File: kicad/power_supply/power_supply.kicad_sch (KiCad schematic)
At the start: 15 parts, among them J1 Conn_WallSocket_Earth, J2 Conn_01x03, J3 Conn_01x04_Pin, SW1 SW_SPST, T1 Transformer_SP_2S

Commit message: Commit
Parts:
- removed J2: Conn_01x03, symbol Connector_Generic:Conn_01x03
- removed J3: Conn_01x04_Pin, symbol Connector:Conn_01x04_Pin
- added C1, C20: 1u, Capacitor_SMD:C_0805_2012Metric_Pad1.18x1.45mm_HandSolder, symbol Device:C
- added C10, C17, C18: 47u, Capacitor_SMD:C_0805_2012Metric_Pad1.18x1.45mm_HandSolder, symbol Device:C
- added C19, C6, C8: 100n, Capacitor_SMD:C_0805_2012Metric_Pad1.18x1.45mm_HandSolder, symbol Device:C
- added C2, C5: 4u7, symbol Device:C
- added C3, C4: C, symbol Device:C
- added C7, C9: 10u, Capacitor_SMD:C_0805_2012Metric_Pad1.18x1.45mm_HandSolder, symbol Device:C
- added D1, D2, D3, D4: D_TVS, symbol Device:D_TVS
- added D6, D7: V<Vgs, symbol Device:D_Zener
- added FB1, FB2: FerriteBead, symbol Device:FerriteBead
- added HS1: Heatsink, symbol Mechanical:Heatsink
- added J2: USB_C_Receptacle_USB2.0, Connector_USB:USB_C_Receptacle_GCT_USB4085, symbol Connector:USB_C_Receptacle_USB2.0
- added J3: Conn_01x03, symbol Connector_Generic:Conn_01x03
- added J4: Conn_02x08_Odd_Even, Connector_PinSocket_2.54mm:PinSocket_2x08_P2.54mm_Vertical, symbol Connector_Generic:Conn_02x08_Odd_Even
- added JP1: Jumper_2_Open, Jumper:SolderJumper-2_P1.3mm_Open_Pad1.0x1.5mm, symbol Jumper:Jumper_2_Open
- added Q1, Q5: PMOS, symbol Simulation_SPICE:PMOS
- added Q2, Q6: NMOS, symbol Simulation_SPICE:NMOS
- added Q3: PNP, symbol Simulation_SPICE:PNP
- added Q4: NPN, symbol Simulation_SPICE:NPN
- added Q7: NPN, Package_TO_SOT_THT:TO-220-3_Vertical, symbol Simulation_SPICE:NPN
- added Q8: PNP, Package_TO_SOT_THT:TO-220-3_Vertical, symbol Simulation_SPICE:PNP
- added R1: 5.1k, Resistor_SMD:R_0805_2012Metric_Pad1.20x1.40mm_HandSolder, symbol Device:R
- added R10, R25, R7: 10k, Resistor_SMD:R_0805_2012Metric_Pad1.20x1.40mm_HandSolder, symbol Device:R
- added R11, R12: 1, symbol Device:R
- added R15, R16: 0R67, symbol Device:R
- added R17, R20: 33k, Resistor_SMD:R_0805_2012Metric_Pad1.20x1.40mm_HandSolder, symbol Device:R
- added R18, R19: 1k, Resistor_SMD:R_0805_2012Metric_Pad1.20x1.40mm_HandSolder, symbol Device:R
- added R2, R5: 1k5, Resistor_SMD:R_0805_2012Metric_Pad1.20x1.40mm_HandSolder, symbol Device:R
- added R21, R22: 3k3, Resistor_SMD:R_0805_2012Metric_Pad1.20x1.40mm_HandSolder, symbol Device:R
- added R23, R24: 100k log, symbol Device:R_Trim
- added R26: 16k, Resistor_SMD:R_0805_2012Metric_Pad1.20x1.40mm_HandSolder, symbol Device:R
- added R3, R4: 22, Resistor_SMD:R_0805_2012Metric_Pad1.20x1.40mm_HandSolder, symbol Device:R
- added R6: 1M, Resistor_SMD:R_0805_2012Metric_Pad1.20x1.40mm_HandSolder, symbol Device:R
- added R8, R9: 100k, Resistor_SMD:R_0805_2012Metric_Pad1.20x1.40mm_HandSolder, symbol Device:R
- added TH1: MOV, symbol Device:Thermistor
- added TH2, TH3: 20R->1R, Capacitor_THT:C_Disc_D9.0mm_W5.0mm_P5.00mm, symbol Device:Thermistor_NTC
- added U1: PCM2707CPJTR, Package_QFP:TQFP-32_7x7mm_P0.8mm, symbol library:PCM2707CPJTR
- added U2: LM317, Package_TO_SOT_SMD:SOT-89-3, symbol Regulator_Linear:LM317L_SOT-89
- added Y1: 12MHz±0.05%, symbol Device:Resonator
- C15: renamed from C5; value 10u -> 47u
- C16: renamed from C6; value 10u -> 47u
- F1: value 250mA -> 160mA; Digikey 507-2270-ND -> 507-1238-ND
- J1: Note (none) -> mains input module with fuse holder
- T1: symbol Device:Transformer_SP_2S -> Transformer:TRANSF6; Digikey 237-1328-ND -> 1295-1074-ND; Spannung ±24Vrms -> 18Vrms
- renumbered C1 to C11, C2 to C12, C3 to C13, C4 to C14, D1 to D5, R1 to R13, R2 to R14
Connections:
- net Earth: now also D1.1 (A1), D2.1 (A1), D3.1 (A1), D4.1 (A1); no longer J1.3 (EARTH)
- net GND: now also T1.7, C17.2, C18.1, J4.10 (Pin_10), J4.13 (Pin_13), J4.3 (Pin_3), J4.4 (Pin_4), R23.1, R24.1, R8.2, R9.1; no longer T1.5 (OUT1B)
- net at F1.1, J1.1 (AC_P): no longer F1.2, T1.1 (IN+)
- net at J1.2 (AC_N), SW1.1 (A): now also C2.2, C4.2, J3.2 (Pin_2), TH1.2
- net at D5.2: now also T1.5, C5.2; no longer T1.7 (OUT2B)
- net at D5.4: now also T1.8, C5.1; no longer T1.4 (OUT1A)
- net at SW1.2 (B): now also T1.4; no longer T1.3 (IN-)
- net at T1.2: now also T1.3
- net +36V renamed +30V
- net +30V: now also J4.2 (Pin_2), Q5.1 (D), Q7.1 (C), R11.2, R21.1, TH2.2; no longer D5.1 (+)
- net -36V renamed -30V
- net -30V: now also J4.6 (Pin_6), Q6.1 (D), Q8.1 (C), R12.2, R22.1, TH3.2; no longer D5.3 (-)
- new net: C18.2, Q8.2 (B), R22.2
- new net: D6.1 (K), Q3.2 (B), Q5.3 (S), R15.1
- new net: D6.2 (A), Q3.1 (C), Q5.2 (G), R17.1, R18.1
- new net: C17.1, Q7.2 (B), R21.2
- new net: R6.2, U1.13 (XTO), Y1.1
- new net: R6.1, U1.12 (XTI), Y1.3
- new net: R5.1, U1.15 (DT)
- new net: C3.2, C4.1, J1.3 (EARTH), J3.3 (Pin_3)
- new net: R25.2, R26.1, U2.1 (ADJ)
- new net: D2.2 (A2), J2.A7 (D-), J2.B7 (D-), R3.1
- new net: C9.1, D5.1 (+), Q1.3 (S), R7.1, TH2.1
- new net: C9.2, Q1.2 (G), R7.2, R8.1
- new net: R19.1, R24.2
- new net: D7.1 (K), Q4.1 (C), Q6.2 (G), R19.2, R20.1
- new net: C2.1, C3.1, F1.2, J3.1 (Pin_1), T1.1, TH1.1
- new net: Q3.3 (E), R15.2
- new net: Q1.1 (D), R11.1
- new net: D3.2 (A2), J2.A6 (D+), J2.B6 (D+), R2.1, R4.1
- new net: D1.2 (A2), FB1.1, J2.A1 (GND), J2.A12 (GND), J2.B1 (GND), J2.B12 (GND)
- new net: FB2.1, J2.A4 (VBUS), J2.A9 (VBUS), J2.B4 (VBUS), J2.B9 (VBUS)
- new net: J2.A5 (CC1), J2.B5 (CC2), R1.1
- new net: J2.S1 (SHIELD), JP1.2 (B)
- new net: C10.1, Q2.2 (G), R10.1, R9.2
- new net: C10.2, D5.3 (-), Q2.3 (S), R10.2, TH3.1
- new net: C8.2, U1.2 (VCCP)
- new net: R3.2, U1.22 (D-)
- new net: R4.2, U1.23 (D+)
- new net: C7.2, U1.32 (VCOM)
- new net: Q2.1 (D), R12.1
- new net: D7.2 (A), Q4.2 (B), Q6.3 (S), R16.1
- new net: Q4.3 (E), R16.2
- new net: R18.2, R23.2
- new net +30Vreg: J4.1 (Pin_1), Q7.3 (E)
- new net +3V3: C20.2, C6.2, J4.9 (Pin_9), R2.2, R25.1, R5.2, U1.10 (TEST), U1.21 (VDD), U2.2 (VO)
- new net -30Vreg: J4.5 (Pin_5), Q8.3 (E)
- new net BCK: J4.15 (Pin_15), U1.19 (FUNC1)
- new net DATA: J4.12 (Pin_12), U1.17 (DOUT)
- new net GNDD: C1.1, C19.1, C20.1, C6.1, C7.1, C8.1, FB1.2, JP1.1 (A), R1.2, R26.2, U1.1 (PGND), U1.16 (PSEL), U1.20 (DGND), U1.25 (ZGND), U1.9 (FSEL), Y1.2
- new net LRCK: J4.11 (Pin_11), U1.5 (FUNC0)
- new net SCK: J4.14 (Pin_14), U1.18 (FUNC2)
- new net SSPND: J4.16 (Pin_16), U1.11 (~{SSPND})
- new net VBUS: C1.2, C19.2, D4.2 (A2), FB2.2, U1.24 (VBUS), U1.3 (HOST), U2.3 (VI)
- no-connect marks 1 -> 15
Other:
- note added: "+3V3 Regulator"
- note added: "21.4Vrms @ no load ≙ 30Vpeak @ no load (sine wave) 18Vrms @ 700mArms ≙ 25.5Vpeak @ 1Apeak (sine wave)"
- note added: "240Vrms ≙ 340Vpeak 57mArms max ≙ 82mApeak max"
- note added: "Capacitance Multiplier"
- note added: "Current Limiter"
- note added: "Inrush Current Limiter"
- note added: "Mains Filtering"
- note added: "Mains Input"
- note added: "Transformer & Rectifier"
- note added: "USB Input"
- note added: "USB to I²S IC"
- note added: "Vbe = 0.63V"
- note added: "cutoff slope too sharp?"
- note added: "filters the supply with capacitance multipliers, not real regulation 0.3-0.5s startup time"
- note added: "handle voltage spike at drain"
- note added: "test X cap"
- note added: "test negative limiter in LTspice 10k -> 11k with higher winding resistance"
- note added: "zener orientation?"
- note removed: "1.2A max"
- note removed: "150mA max"
- note removed: "input module for socket and fuse"
- moved on the sheet: C11, C12, C13, C14, C15, C16, D5, J1, R13, R14, SW1

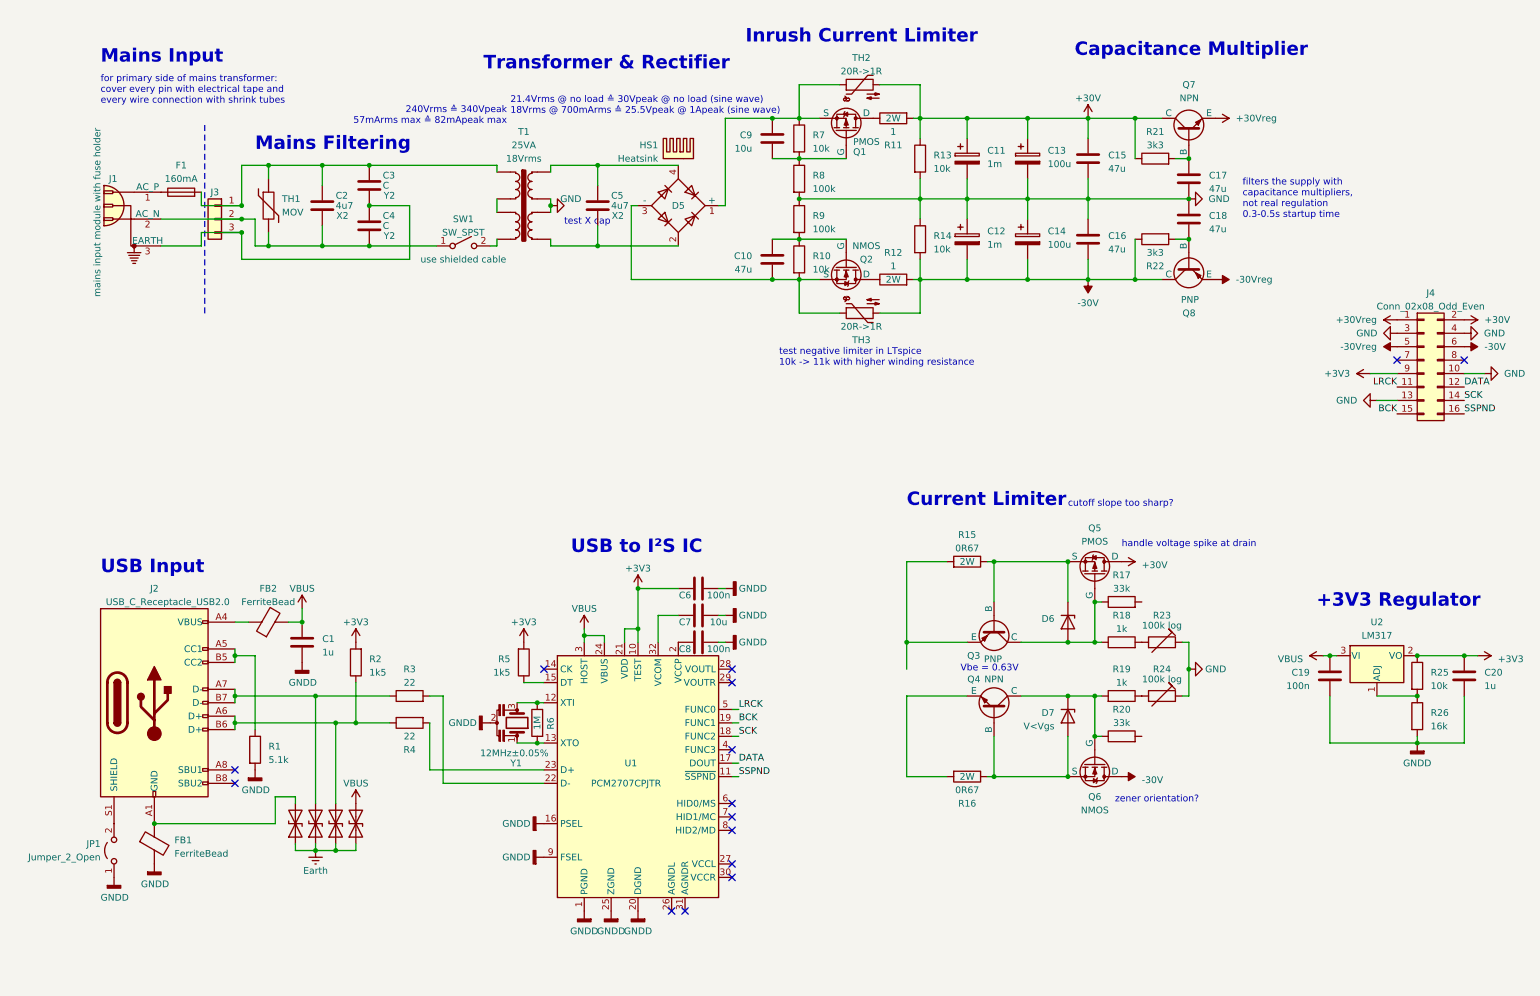
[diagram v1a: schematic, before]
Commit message: completed power supply footprints and placement
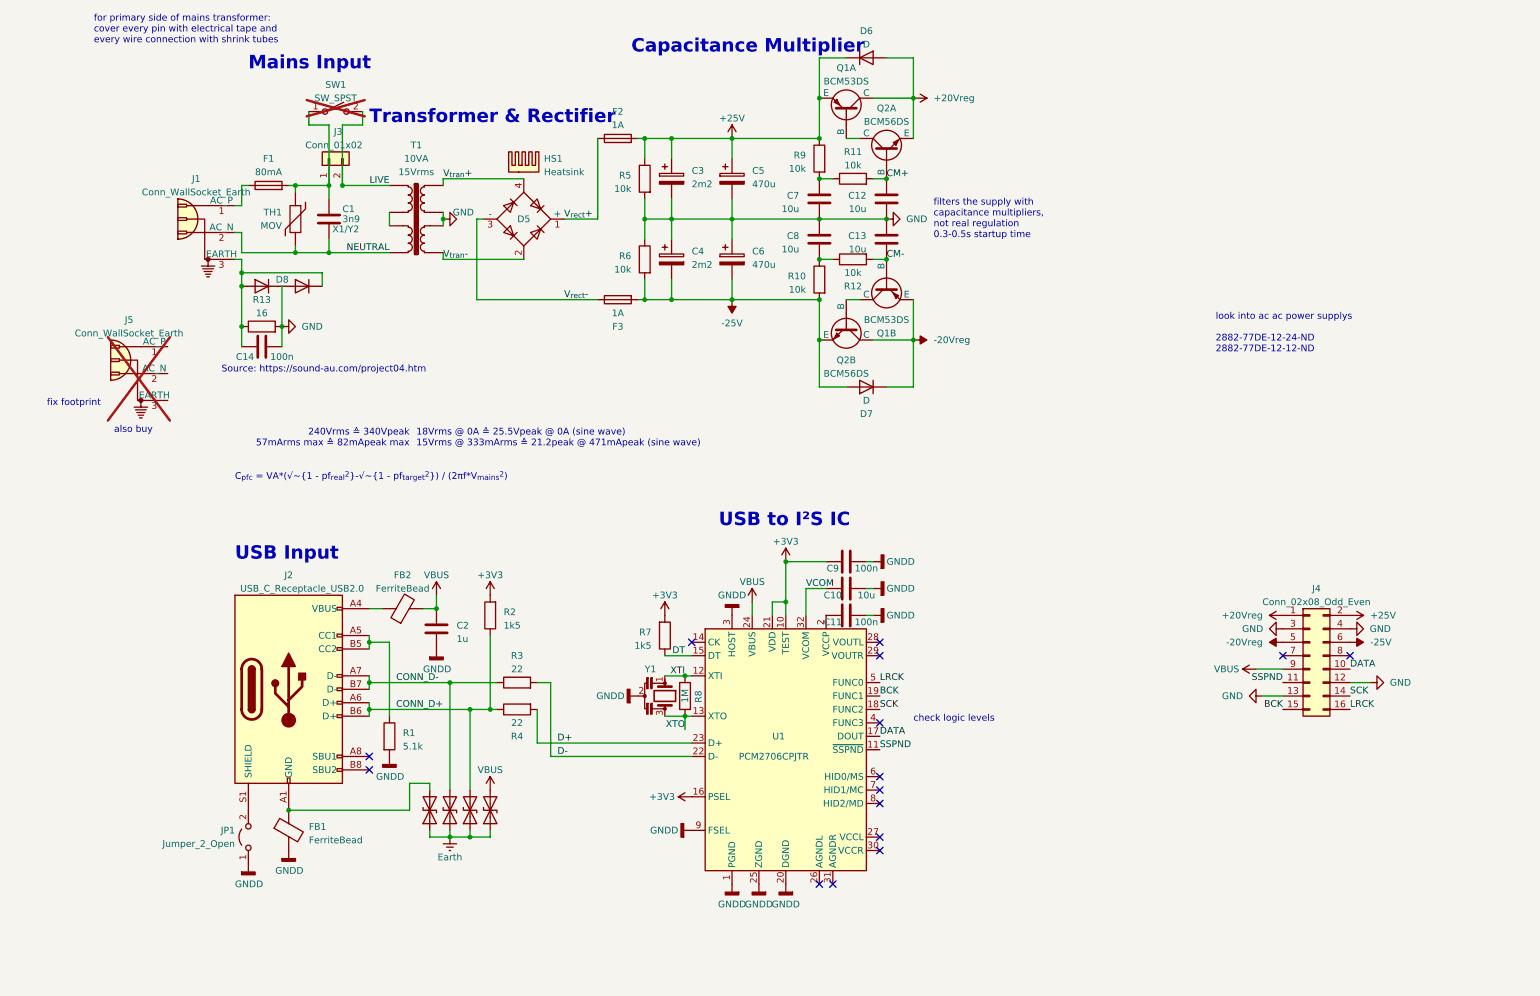
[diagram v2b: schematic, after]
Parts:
- removed C10, C15, C16, C18: 47u, Capacitor_SMD:C_0805_2012Metric_Pad1.18x1.45mm_HandSolder, symbol Device:C
- removed C14: 100u, symbol Device:C_Polarized
- removed C19: 100n, Capacitor_SMD:C_0805_2012Metric_Pad1.18x1.45mm_HandSolder, symbol Device:C
- removed C20: 1u, Capacitor_SMD:C_0805_2012Metric_Pad1.18x1.45mm_HandSolder, symbol Device:C
- removed C3, C4: C, symbol Device:C
- removed C5: 4u7, symbol Device:C
- removed C9: 10u, Capacitor_SMD:C_0805_2012Metric_Pad1.18x1.45mm_HandSolder, symbol Device:C
- removed D6, D7: V<Vgs, symbol Device:D_Zener
- removed J3: Conn_01x03, symbol Connector_Generic:Conn_01x03
- removed Q1, Q5: PMOS, symbol Simulation_SPICE:PMOS
- removed Q2, Q6: NMOS, symbol Simulation_SPICE:NMOS
- removed Q3: PNP, symbol Simulation_SPICE:PNP
- removed Q4: NPN, symbol Simulation_SPICE:NPN
- removed Q7: NPN, Package_TO_SOT_THT:TO-220-3_Vertical, symbol Simulation_SPICE:NPN
- removed Q8: PNP, Package_TO_SOT_THT:TO-220-3_Vertical, symbol Simulation_SPICE:PNP
- removed R15, R16: 0R67, symbol Device:R
- removed R17, R20: 33k, Resistor_SMD:R_0805_2012Metric_Pad1.20x1.40mm_HandSolder, symbol Device:R
- removed R18, R19: 1k, Resistor_SMD:R_0805_2012Metric_Pad1.20x1.40mm_HandSolder, symbol Device:R
- removed R21, R22: 3k3, Resistor_SMD:R_0805_2012Metric_Pad1.20x1.40mm_HandSolder, symbol Device:R
- removed R23, R24: 100k log, symbol Device:R_Trim
- removed R25, R7: 10k, Resistor_SMD:R_0805_2012Metric_Pad1.20x1.40mm_HandSolder, symbol Device:R
- removed R26: 16k, Resistor_SMD:R_0805_2012Metric_Pad1.20x1.40mm_HandSolder, symbol Device:R
- removed R8: 100k, Resistor_SMD:R_0805_2012Metric_Pad1.20x1.40mm_HandSolder, symbol Device:R
- removed TH2, TH3: 20R->1R, Capacitor_THT:C_Disc_D9.0mm_W5.0mm_P5.00mm, symbol Device:Thermistor_NTC
- removed U2: LM317, Package_TO_SOT_SMD:SOT-89-3, symbol Regulator_Linear:LM317L_SOT-89
- added C13, C7, C8: 10u, Capacitor_SMD:C_1206_3216Metric_Pad1.33x1.80mm_HandSolder, symbol Device:C
- added C14: 100n, Capacitor_SMD:C_1206_3216Metric_Pad1.33x1.80mm_HandSolder, symbol Device:C
- added C6: 470u, Capacitor_THT:CP_Radial_D10.0mm_P5.00mm, symbol Device:C_Polarized
- added D6, D7: D, Diode_SMD:D_SOD-323_HandSoldering, symbol Device:D
- added D8: ~, Package_TO_SOT_SMD:SOT-23-3, symbol library:Dual_Diode_Array
- added F2, F3: 1A, Fuse:Fuse_1206_3216Metric_Pad1.42x1.75mm_HandSolder, symbol Device:Fuse
- added J3: Conn_01x02, library:WAGO_2086-11X2, symbol Connector_Generic:Conn_01x02
- added J5: Conn_WallSocket_Earth, library:WallSocket_Adam-Tech, symbol Connector:Conn_WallSocket_Earth
- added Q1: BCM53DS, Package_SO:SC-74-6_1.5x2.9mm_P0.95mm, symbol library:Dual-PNP
- added Q2: BCM56DS, Package_SO:SC-74-6_1.5x2.9mm_P0.95mm, symbol library:Dual-NPN
- added R13: 16, Resistor_SMD:R_1206_3216Metric_Pad1.30x1.75mm_HandSolder, symbol Device:R
- C1: renamed from C2; value 4u7 -> 3n9; footprint (none) -> Capacitor_THT:C_Disc_D10.5mm_W5.0mm_P7.50mm; Digikey (none) -> BC3311-ND; Note X2 -> X1/Y2; Note2 (none) -> Value: https://electronics.stackexchange.com/q/270857
- C10: renamed from C7; footprint Capacitor_SMD:C_0805_2012Metric_Pad1.18x1.45mm_HandSolder -> Capacitor_SMD:C_1206_3216Metric_Pad1.33x1.80mm_HandSolder; Digikey (none) -> 1276-3100-1-ND
- C11: renamed from C8; footprint Capacitor_SMD:C_0805_2012Metric_Pad1.18x1.45mm_HandSolder -> Capacitor_SMD:C_1206_3216Metric_Pad1.33x1.80mm_HandSolder
- C12: renamed from C17; value 47u -> 10u; footprint Capacitor_SMD:C_0805_2012Metric_Pad1.18x1.45mm_HandSolder -> Capacitor_SMD:C_1206_3216Metric_Pad1.33x1.80mm_HandSolder; Digikey (none) -> 1276-3100-1-ND
- C2: renamed from C1; footprint Capacitor_SMD:C_0805_2012Metric_Pad1.18x1.45mm_HandSolder -> Capacitor_SMD:C_1206_3216Metric_Pad1.33x1.80mm_HandSolder
- C3: renamed from C11; value 1m -> 2m2; footprint (none) -> Capacitor_THT:CP_Radial_D12.5mm_P5.00mm; Digikey (none) -> 1189-3669-ND
- C4: renamed from C12; value 1m -> 2m2; footprint (none) -> Capacitor_THT:CP_Radial_D12.5mm_P5.00mm; Digikey (none) -> 1189-3669-ND
- C5: renamed from C13; value 100u -> 470u; footprint (none) -> Capacitor_THT:CP_Radial_D10.0mm_P5.00mm; Digikey (none) -> 493-5931-1-ND
- C9: renamed from C6; footprint Capacitor_SMD:C_0805_2012Metric_Pad1.18x1.45mm_HandSolder -> Capacitor_SMD:C_1206_3216Metric_Pad1.33x1.80mm_HandSolder
- D5: footprint (none) -> Diode_SMD:Diode_Bridge_Vishay_MBLS; Digikey 1514-CBRLDSH2-100TR13PBFREECT-ND -> 3757-TS360ILS_R1_00001CT-ND
- F1: value 160mA -> 80mA; footprint (none) -> Fuse:Fuse_Littelfuse_372_D8.50mm; Digikey 507-1238-ND -> 486-1461-ND
- HS1: footprint (none) -> library:Heatsink_10x10
- J1: footprint (none) -> library:WallSocket_Schurter_6160.0003; Digikey Q201-ND -> 486-4032-ND; Note mains input module with fuse holder -> (none)
- R1, R10, R2, R3, R4: footprint Resistor_SMD:R_0805_2012Metric_Pad1.20x1.40mm_HandSolder -> Resistor_SMD:R_1206_3216Metric_Pad1.30x1.75mm_HandSolder
- R11, R12: value 1 -> 10k; footprint (none) -> Resistor_SMD:R_1206_3216Metric_Pad1.30x1.75mm_HandSolder; Power 2W -> (none)
- R5: renamed from R13; footprint Resistor_SMD:R_0805_2012Metric_Pad1.20x1.40mm_HandSolder -> Resistor_SMD:R_1206_3216Metric_Pad1.30x1.75mm_HandSolder
- R6: renamed from R14; footprint Resistor_SMD:R_0805_2012Metric_Pad1.20x1.40mm_HandSolder -> Resistor_SMD:R_1206_3216Metric_Pad1.30x1.75mm_HandSolder
- R7: renamed from R5; footprint Resistor_SMD:R_0805_2012Metric_Pad1.20x1.40mm_HandSolder -> Resistor_SMD:R_1206_3216Metric_Pad1.30x1.75mm_HandSolder
- R8: renamed from R6; footprint Resistor_SMD:R_0805_2012Metric_Pad1.20x1.40mm_HandSolder -> Resistor_SMD:R_1206_3216Metric_Pad1.30x1.75mm_HandSolder
- R9: value 100k -> 10k; footprint Resistor_SMD:R_0805_2012Metric_Pad1.20x1.40mm_HandSolder -> Resistor_SMD:R_1206_3216Metric_Pad1.30x1.75mm_HandSolder
- SW1: Digikey (none) -> 360-1722-ND; Note use shielded cable -> (none); now not fitted
- T1: value Transformer_SP_2S -> 70043K; footprint (none) -> library:Talema_Transformer_2P2S_10VA; Digikey 1295-1074-ND -> 1295-1043-ND; Leistung 25VA -> 10VA; Spannung 18Vrms -> 15Vrms
- TH1: footprint (none) -> Varistor:RV_Disc_D12mm_W6.3mm_P7.5mm; Digikey (none) -> P16674-ND
- U1: value PCM2707CPJTR -> PCM2706CPJTR
- Y1: footprint (none) -> library:Resonator_Murata
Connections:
- net +3V3: now also U1.16 (PSEL); no longer J4.9 (Pin_9)
- net DATA: now also J4.10 (Pin_10); no longer J4.12 (Pin_12)
- net GND: now also J4.12 (Pin_12), C13.1, C14.1, C6.1, C7.2, C8.1, D8.3 (C/A), R13.2; no longer J4.10 (Pin_10), R9.1
- net GNDD: now also U1.3 (HOST); no longer U1.16 (PSEL)
- net LRCK: now also J4.16 (Pin_16); no longer J4.11 (Pin_11)
- net SSPND: now also J4.11 (Pin_11); no longer J4.16 (Pin_16)
- net VBUS: now also J4.9 (Pin_9); no longer U1.3 (HOST)
- net CM+: now reaches C12.1
- net CM+: now also R11.2, Q2.1 (B)
- net XTO: now reaches R8.2, U1.13 (XTO)
- net XTO: now also Y1.3; no longer Y1.1
- net XTI: now reaches R8.1, U1.12 (XTI)
- net XTI: now also Y1.1; no longer Y1.3
- net DT: now reaches R7.1, U1.15 (DT)
- net NEUTRAL: now reaches C1.2, J1.2 (AC_N), TH1.2
- net NEUTRAL: now also T1.4; no longer SW1.1 (A)
- net at J1.3 (EARTH): now also C14.2, D8.1 (A), D8.2 (C), R13.1
- net CONN_D-: now reaches D2.2 (A2), J2.A7 (D-), J2.B7 (D-), R3.1
- net V_{rect}+: now reaches D5.1 (+)
- net V_{rect}+: now also F2.1
- net at C1.1, F1.2, TH1.1: now also SW1.1 (A), J3.1 (Pin_1); no longer T1.1
- net at R11.1: now also R9.2, C7.1
- net CONN_D+: now reaches D3.2 (A2), J2.A6 (D+), J2.B6 (D+), R2.1, R4.1
- net at R10.1: now also R12.1, C8.2; no longer R9.2
- net -25V: now reaches R10.2
- net -25V: now also C4.2, J4.6 (Pin_6), R6.2, C6.2, D7.2 (A), F3.2, Q2.4 (E); no longer D5.3 (-)
- net V_{tran}-: now reaches D5.2, T1.5
- net V_{tran}+: now reaches D5.4, T1.8
- net D-: now reaches R3.2, U1.22 (D-)
- net D+: now reaches R4.2, U1.23 (D+)
- net VCOM: now reaches C10.2, U1.32 (VCOM)
- net LIVE: now reaches SW1.2 (B)
- net LIVE: now also T1.1, J3.2 (Pin_2); no longer T1.4
- net +30V renamed +25V
- net +25V: now also R9.1, D6.1 (K), F2.2, Q1.5 (E); no longer R11.2
- net +30Vreg renamed +20Vreg
- net +20Vreg: now also D6.2 (A), Q1.6 (C), Q2.5 (E)
- removed net -30V: C4.2, J4.6 (Pin_6), R12.2, R6.2
- net -30Vreg renamed -20Vreg
- net -20Vreg: now also D7.1 (K), Q1.4 (E), Q2.3 (C)
- new net: Q1.1 (B), Q2.6 (C)
- new net: Q1.3 (C), Q2.2 (B)
- new net CM-: C13.2, Q1.2 (B), R12.2
- new net V_{rect}-: D5.3 (-), F3.1
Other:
- note added: "18Vrms @ 0A ≙ 25.5Vpeak @ 0A (sine wave) 15Vrms @ 333mArms ≙ 21.2peak @ 471mApeak (sine wave)"
- note added: "C_{pfc} = VA*(√~{1 - pf_{real}^{2}}-√~{1 - pf_{target}^{2}}) / (2πf*V_{mains}^{2})"
- note added: "Source: https://sound-au.com/project04.htm"
- note added: "also buy"
- note added: "check logic levels"
- note added: "fix footprint"
- note added: "look into ac ac power supplys 2882-77DE-12-24-ND 2882-77DE-12-12-ND"
- note removed: "+3V3 Regulator"
- note removed: "21.4Vrms @ no load ≙ 30Vpeak @ no load (sine wave) 18Vrms @ 700mArms ≙ 25.5Vpeak @ 1Apeak (sine wave)"
- note removed: "Current Limiter"
- note removed: "Inrush Current Limiter"
- note removed: "Mains Filtering"
- note removed: "Vbe = 0.63V"
- note removed: "cutoff slope too sharp?"
- note removed: "handle voltage spike at drain"
- note removed: "test X cap"
- note removed: "test negative limiter in LTspice 10k -> 11k with higher winding resistance"
- note removed: "zener orientation?"
- moved on the sheet: C1, C10, C11, C12, C2, C3, C4, C5, C9, D5, FB1, FB2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
